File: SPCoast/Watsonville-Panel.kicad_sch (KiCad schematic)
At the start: 8 parts, among them U16034 0x2D

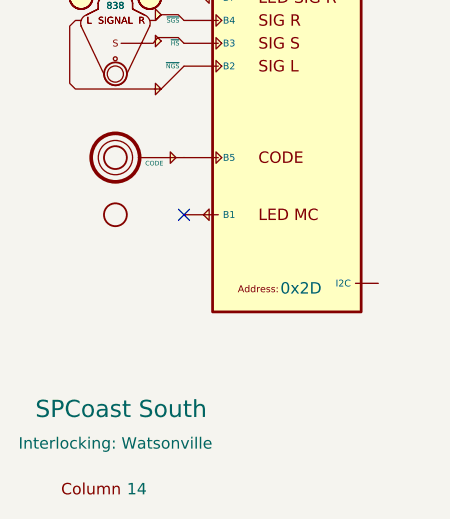
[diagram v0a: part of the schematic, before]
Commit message: feat(kicad): Sargent, Watsonville, Corporal, Christopher as local units with the four ports; all panels on the desk bus
SPCoast/edits/2026-10-21-local-units.py (owner's instruction 2026-10-21: assume each is like
Sargent, a local cpNode-Xiao with I2C I/O; prepopulate, tidy by hand later).

- Watsonville, Corporal, Christopher: a Processor '<unit>' (cpNode-Xiao) above the Interlocking,
  Host wired to it; an IOBus port on its bus pin. Sargent: IOBus port on Proc6 with its three
  expanders labelled onto it, and a Host port.
- Every Panel box gains an I2C pin carrying the OfficeIOBus port; every MAX7313 bus pin on the
  four panels is labelled I2C.
- South-cTc: the three units host themselves (their drops from the SPCoastApp host line removed,
  the line shortened to the Gilroy pair); the four boxes gain IOBus and OfficeIOBus (Sargent also
  Host), Host and IOBus no-connected, OfficeIOBus dropped onto the office line, extended right
  with junctions.

Verified: --check on production/local-units-before.net vs -after.net: desk bus = JohnCTC plus all
14 panel expanders; each unit's Host net is its own processor; SPCoastApp hosts Gilroy Caltrain,
Gilroy Interchange and the two I/O transports; Sargent's bus = Proc6 plus three expanders;
MQTT, TIMECODE, CMRInet, JMRI_MQTT unchanged; nothing else changed; parts added Proc8-10 only.
ERC: 0 violations. Rendered South-cTc and Sargent and inspected.

Co-Authored-By: Claude Fable 5.1 <noreply@anthropic.com>
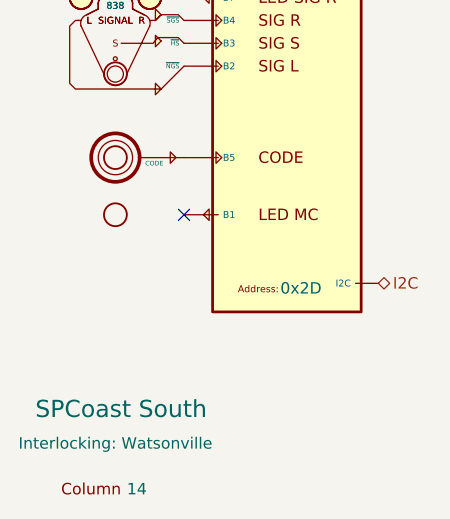
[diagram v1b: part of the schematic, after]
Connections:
- net I2C: now reaches U16034.17 (I2C)
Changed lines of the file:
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@@
 		(at 87.63 104.14)
+	)
+	(hierarchical_label "I2C"
+		(shape bidirectional)
+		(at 109.22 111.76 0)
+		(effects
+			(font
+				(size 1.27 1.27)
+			)
+			(justify left)
+		)
 	)
 	(symbol
